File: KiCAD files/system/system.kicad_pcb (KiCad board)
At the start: 2 copper layers, 104.1 x 61 mm, 14 parts, among them J1 Input, J2 Conn_01x04_Female, SW1 SW_Push, U1 ATmega328P-P, Y1 Crystal

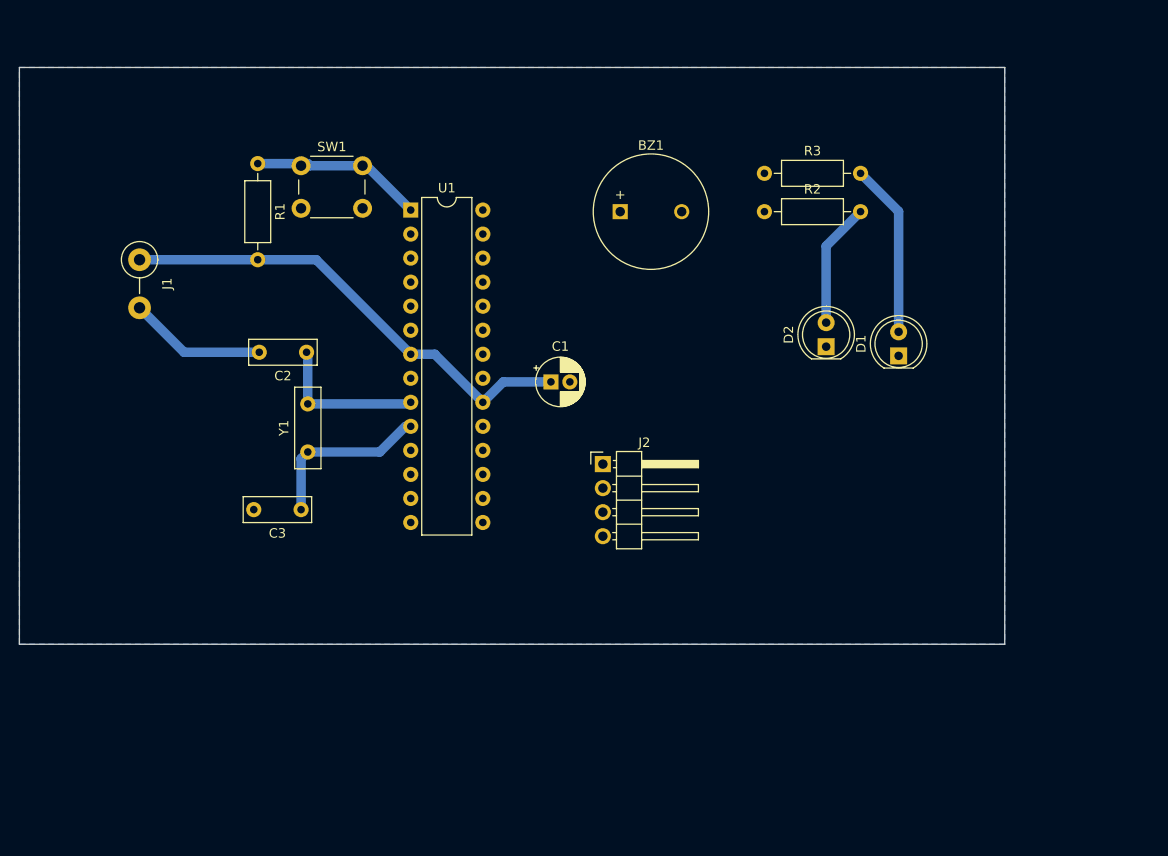
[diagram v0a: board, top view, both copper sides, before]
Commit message: edited system side pcb
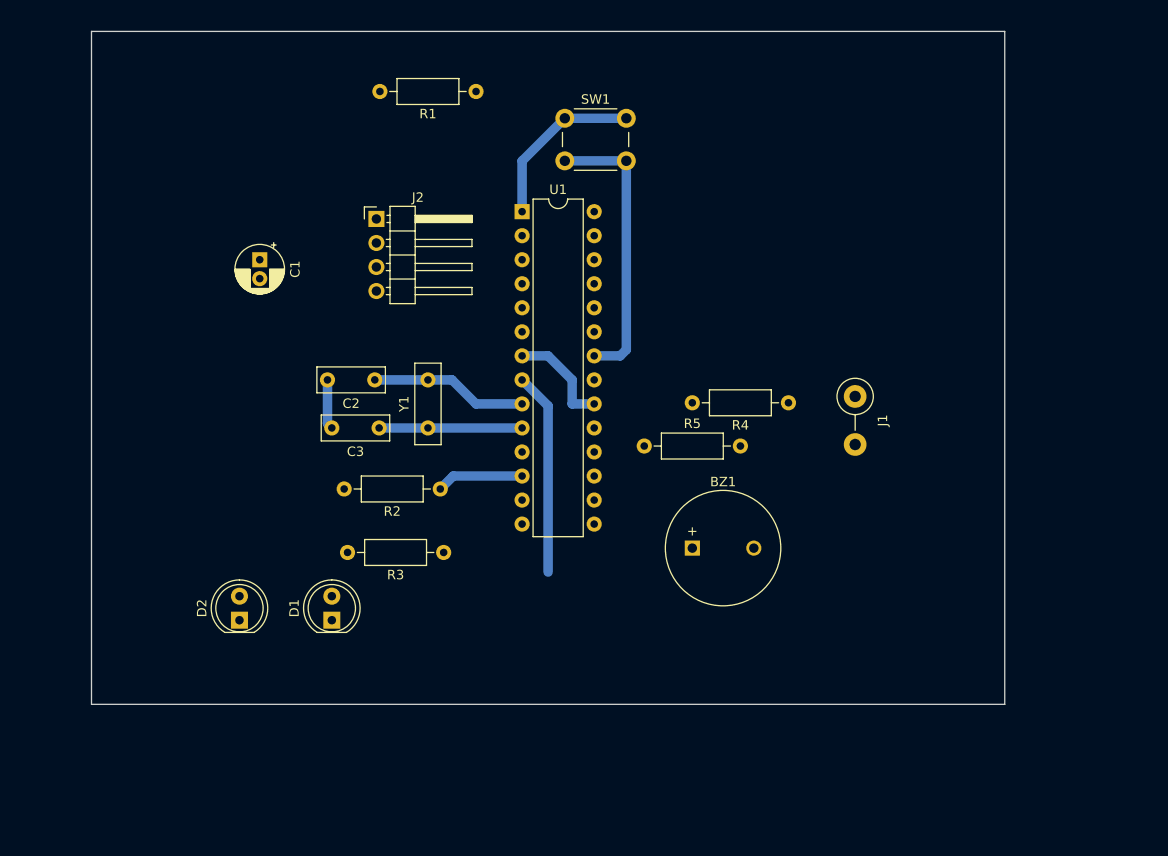
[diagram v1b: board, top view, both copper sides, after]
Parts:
- added R4: 5.1kR, Resistor_THT:R_Axial_DIN0207_L6.3mm_D2.5mm_P10.16mm_Horizontal, F.Cu at (167.6, 88.8)
- added R5: 10kR, Resistor_THT:R_Axial_DIN0207_L6.3mm_D2.5mm_P10.16mm_Horizontal, F.Cu at (152.4, 93.3)
- moved J1 77.0 mm to (174.7, 88.1)
- moved D2 68.4 mm to (109.6, 111.8)
- moved D1 66.1 mm to (119.4, 111.8)
- moved R3 52.5 mm to (131.2, 104.6), turned to 180 degrees
- moved R2 45.1 mm to (130.8, 97.9), turned to 180 degrees
- moved BZ1 36.4 mm to (157.5, 104.1)
- moved J2 35.3 mm to (124.1, 69.3)
- moved C1 33.4 mm to (111.8, 73.7), turned to -90 degrees
- moved SW1 28.3 mm to (144.0, 58.7)
- moved R1 24.3 mm to (134.6, 55.9), turned to 180 degrees
- moved Y1 13.0 mm to (129.5, 91.4)
- moved C3 11.9 mm to (124.4, 91.4)
- moved U1 11.8 mm to (139.5, 68.6)
- moved C2 7.78 mm to (123.9, 86.4)
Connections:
- BZ1 pad 1: unconnected-(BZ1-Pad1) -> /PB1
- C1 pad 1: +5V -> +3.3V
- J2 pad 1: unconnected-(J2-Pad1) -> +3.3V
- J2 pad 2: unconnected-(J2-Pad2) -> /data
- J2 pad 3: unconnected-(J2-Pad3) -> /data
- J2 pad 4: unconnected-(J2-Pad4) -> GND
- R1 pad 2: +5V -> +3.3V
- R2 pad 1: unconnected-(R2-Pad1) -> /PD6
- R3 pad 1: unconnected-(R3-Pad1) -> /PD7
- U1 pad 12: unconnected-(U1-Pad12) -> /PD6
- U1 pad 13: unconnected-(U1-Pad13) -> /PD7
- U1 pad 15: unconnected-(U1-Pad15) -> /PB1
- U1 pad 2: unconnected-(U1-Pad2) -> /data
- U1 pad 20: +5V -> +3.3V
- U1 pad 7: +5V -> +3.3V
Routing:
- net +5V: track 50.6 -> 0.00 mm
- net GND: track 14.6 -> 56.9 mm
- net Net-(D1-Pad2): track 18.4 -> 0.00 mm
- net Net-(D2-Pad2): track 13.2 -> 0.00 mm
- net +3.3V: track 0.00 -> 11.2 mm
- net /PD6: track 0.00 -> 9.21 mm
- net Net-(C3-Pad1): track 18.4 -> 15.1 mm
- removed copper zone on B.Cu, net GND
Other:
- board size 104.1 x 61 mm -> 96.5 x 71.1 mm

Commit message: edited system pcb
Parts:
- C1: value C_Polarized -> 10u
- J2: value Conn_01x04_Female -> Conn_01x06_Female; footprint Connector_PinHeader_2.54mm:PinHeader_1x04_P2.54mm_Horizontal -> Connector_PinHeader_2.54mm:PinHeader_1x06_P2.54mm_Vertical
- R1: value R -> 10k
- R2, R3: value R -> 440
- moved D2 86.6 mm to (196.2, 108.8), turned to 180 degrees
- moved D1 77.6 mm to (196.3, 101.2), turned to 180 degrees
- moved C1 72.8 mm to (180.3, 98.0), turned to 0 degrees
- moved J1 58.4 mm to (124.4, 58.4)
- moved R2 48.0 mm to (177.8, 107.9), turned to 0 degrees
- moved R3 46.6 mm to (177.8, 102.6), turned to 0 degrees
- moved R4 44.4 mm to (135.2, 58.4), turned to 0 degrees
- moved C3 28.8 mm to (149.5, 105.5)
- moved R5 27.6 mm to (164.5, 68.6)
- moved C2 26.3 mm to (149.2, 93.7)
- moved BZ1 25.4 mm to (177.8, 119.4)
- moved R1 24.8 mm to (156.2, 68.2), turned to 90 degrees
- moved Y1 22.9 mm to (149.9, 102.0)
- moved U1 20.1 mm to (157.3, 77.9)
- moved J2 13.2 mm to (137.2, 71.1)
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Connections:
- J2 pad 1: +3.3V -> unconnected-(J2-Pad1)
- J2 pad 2: /data -> +5V
- J2 pad 3: /data -> GND
- J2 pad 4: GND -> /txd
- U1 pad 12: /PD6 -> unconnected-(U1-Pad12)
- U1 pad 13: /PD7 -> unconnected-(U1-Pad13)
- U1 pad 17: unconnected-(U1-Pad17) -> /PD6
- U1 pad 18: unconnected-(U1-Pad18) -> /PD7
- U1 pad 2: /data -> /txd
- U1 pad 3: unconnected-(U1-Pad3) -> /rxd
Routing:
- net GND: track 56.9 -> 273.6 mm
- net +3.3V: track 11.2 -> 77.6 mm
- net +5V: track 0.00 -> 32.0 mm
- net /txd: track 0.00 -> 20.8 mm
- net /rxd: track 0.00 -> 20.8 mm
- net /PB1: track 0.00 -> 16.4 mm
- net /PD7: track 0.21 -> 13.2 mm
- net Net-(D1-Pad2): track 0.00 -> 6.39 mm
- net Net-(D2-Pad2): track 0.00 -> 6.06 mm
- net Net-(R1-Pad1): track 18.7 -> 24.3 mm
- net Net-(C2-Pad1): track 16.6 -> 11.4 mm
- net /PD6: track 9.21 -> 13.7 mm
- net Net-(C3-Pad1): track 15.1 -> 11.6 mm
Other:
- board size 96.5 x 71.1 mm -> 96.5 x 86.4 mm
- board text added: "FALL DETECTION SYSTEM AKANKSHA GIRI(076BEI004) DEVRAJ PARAJULI(076BEI013) PRAYAG MAN MANE(076BEI027) SANIM KUMAR KHATRI(076BEI037)"

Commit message: final draft of the system side pcb
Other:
- board size 96.5 x 86.4 mm -> 91.4 x 78.7 mm
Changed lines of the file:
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@@
     )
   )
-  (gr_rect (start 205.74 134.62) (end 109.22 48.26) (layer "Edge.Cuts") (width 0.1) (fill none))
+  (gr_rect (start 203.2 132.08) (end 111.76 53.34) (layer "Edge.Cuts") (width 0.1) (fill none))
   (gr_text "FALL DETECTION SYSTEM\nAKANKSHA GIRI(076BEI004)\nDEVRAJ PARAJULI(076BEI013)\nPRAYAG MAN MANE(076BEI027)\nSANIM KUMAR KHATRI(076BEI037)" (at 132.08 121.92) (layer "F.SilkS")
     (effects (font (size 1.2 1.2) (thickness 0.15)))
